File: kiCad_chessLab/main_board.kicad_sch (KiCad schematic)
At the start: 3 parts, among them IC1 ESP32-C6-WROOM-1-N8, J1 TYPE-C-31-M-12

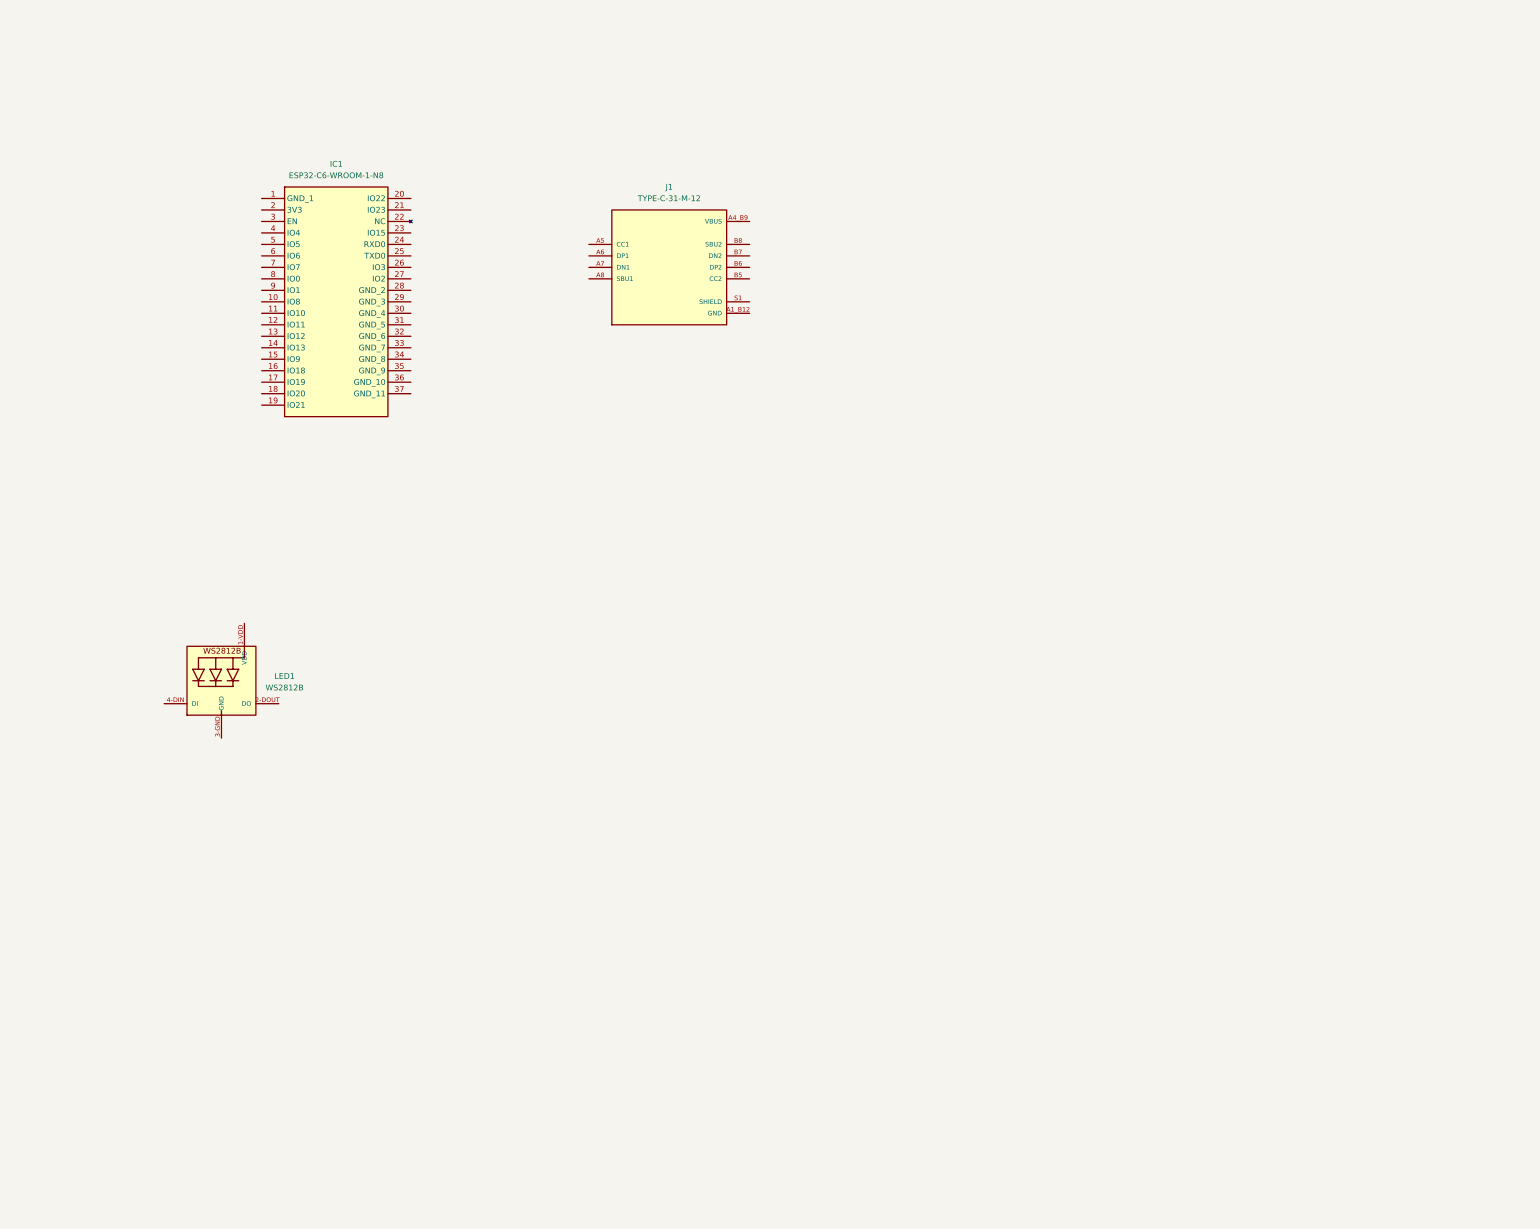
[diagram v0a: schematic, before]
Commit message: Creation des Cellules et Fonctions de Multiplexage
Organisation du projet KiCad en SousPages

Creation des Fonctions Cell: Gestion individuelle de une case

Row: Multiplexage de 8 cell

Main Board:
Liaisons avec ESP32C6
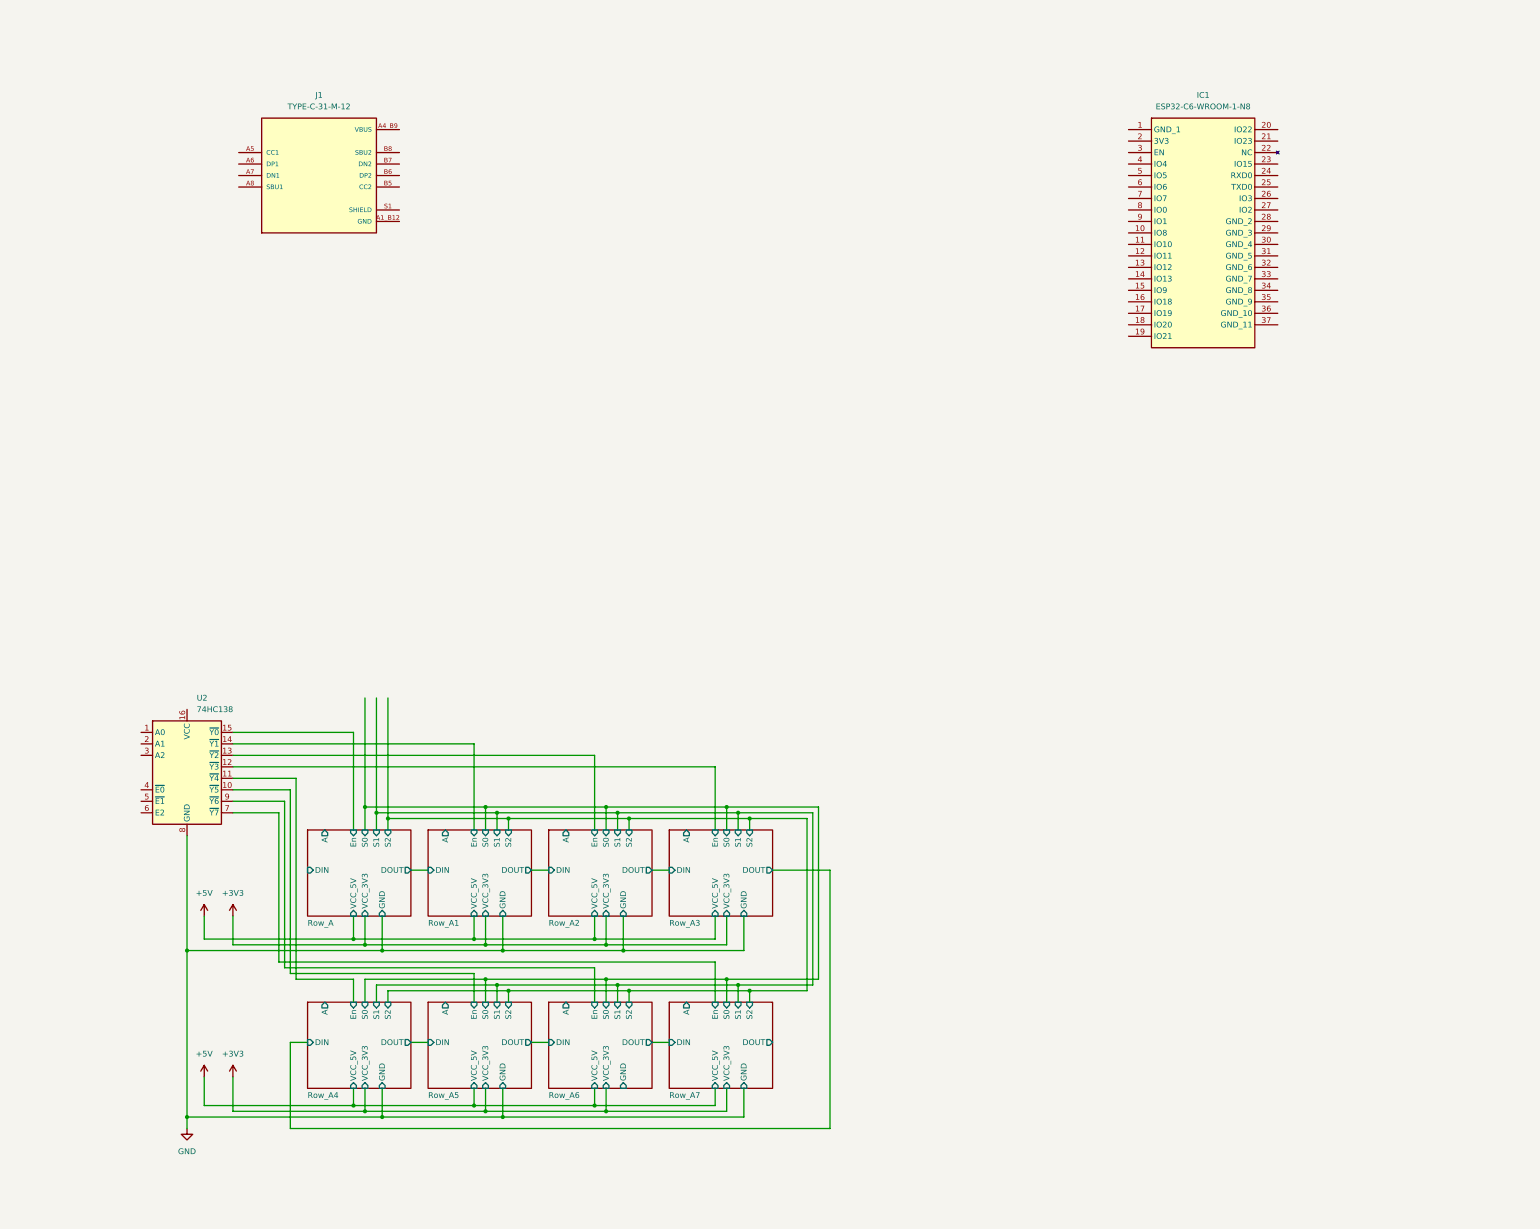
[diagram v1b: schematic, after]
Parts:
- removed LED1: WS2812B, symbol chessLab-symbols:WS2812B
- added U2: 74HC138, Package_SO:SOIC-16_3.9x9.9mm_P1.27mm, symbol 74xx:74HC138
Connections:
- net GND: now also U2.8 (GND)
- new net Row_A/En: U2.15 (~{Y0})
- new net Row_A1/En: U2.14 (~{Y1})
- new net Row_A2/En: U2.13 (~{Y2})
- new net Row_A3/En: U2.12 (~{Y3})
- new net Row_A4/En: U2.11 (~{Y4})
- new net Row_A5/En: U2.10 (~{Y5})
- new net Row_A6/En: U2.9 (~{Y6})
- new net Row_A7/En: U2.7 (~{Y7})
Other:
- added sheet Row_A (row.kicad_sch)
- added sheet Row_A1 (row.kicad_sch)
- added sheet Row_A2 (row.kicad_sch)
- added sheet Row_A3 (row.kicad_sch)
- added sheet Row_A4 (row.kicad_sch)
- added sheet Row_A5 (row.kicad_sch)
- added sheet Row_A6 (row.kicad_sch)
- added sheet Row_A7 (row.kicad_sch)
- moved on the sheet: IC1, J1

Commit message: KiCad Bug Fix
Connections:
- net +3V3: now also U2.16 (VCC)
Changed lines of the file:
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@@
+	(wire
+		(pts
+			(xy 53.34 163.83) (xy 53.34 170.18)
+		)
+		(stroke
+			(width 0)
+			(type default)
+		)
+	)
 	(wire
 		(pts
@@
 		)
 	)
+	(symbol
+		(lib_id "power:+3V3")
+		(at 53.34 163.83 0)
+		(unit 1)
+		(exclude_from_sim no)
+		(in_bom yes)
+		(on_board yes)
+		(dnp no)
+		(fields_autoplaced yes)
+		(property "Reference" "#PWR06"
+			(at 53.34 167.64 0)
+			(effects
+				(font
+					(size 1.27 1.27)
+				)
+				(hide yes)
+			)
+		)
+		(property "Value" "+3V3"
+			(at 53.34 158.75 0)
+			(effects
+				(font
+					(size 1.27 1.27)
+				)
+			)
+		)
+		(property "Footprint" ""
+			(at 53.34 163.83 0)
+			(effects
+				(font
+					(size 1.27 1.27)
+				)
+				(hide yes)
+			)
+		)
+		(property "Datasheet" ""
+			(at 53.34 163.83 0)
+			(effects
+				(font
+					(size 1.27 1.27)
+				)
+				(hide yes)
+			)
+		)
+		(property "Description" "Power symbol creates a global label with name \"+3V3\""
+			(at 53.34 163.83 0)
+			(effects
+				(font
+					(size 1.27 1.27)
+				)
+				(hide yes)
+			)
+		)
+		(pin "1"
+		)
+		(instances
+			(project "kiCad_chessLab"
+				(path "/767acb05-88fd-4294-8dd3-73f8ac75b0d1/879e1270-2f10-48e2-adb9-8c8e9c331030"
+					(reference "#PWR06")
+					(unit 1)
+				)
+			)
+		)
+	)

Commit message: Main Board update
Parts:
- added BOOT, RST: B3U-1000P, B3U-1000P, symbol chessLab-symbols:B3U-1000P
- added C66: 100nF, Capacitor_SMD:C_0603_1608Metric_Pad1.08x0.95mm_HandSolder, symbol Device:C
- added C67: 100uF, Capacitor_SMD:C_0603_1608Metric_Pad1.08x0.95mm_HandSolder, symbol Device:C
- added C68: 10uF, Capacitor_SMD:C_0603_1608Metric_Pad1.08x0.95mm_HandSolder, symbol Device:C
- added J2: PWR, CONN4_1048_KEY, symbol chessLab-symbols:1048
- added J3: DATA, CONN4_1048_KEY, symbol chessLab-symbols:1048
- added R1: 33, Resistor_SMD:R_0603_1608Metric_Pad0.98x0.95mm_HandSolder, symbol Device:R
- added R11, R8: 100k, Resistor_SMD:R_0603_1608Metric_Pad0.98x0.95mm_HandSolder, symbol Device:R
- added R115, R116: 5.1k, Resistor_SMD:R_0603_1608Metric_Pad0.98x0.95mm_HandSolder, symbol Device:R
- added R2, R4, R6: 10k, Resistor_SMD:R_0603_1608Metric_Pad0.98x0.95mm_HandSolder, symbol Device:R
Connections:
- net +3V3: now also IC1.2 (3V3), U2.6 (E2), C66.2, C67.2, C68.2, J2.3, R2.2, R4.2
- net +5V: now also J2.2
- net GND: now also IC1.1 (GND_1), IC1.28 (GND_2), IC1.29 (GND_3), IC1.30 (GND_4), IC1.31 (GND_5), IC1.32 (GND_6), IC1.33 (GND_7), IC1.34 (GND_8), IC1.35 (GND_9), IC1.36 (GND_10), IC1.37 (GND_11), J1.S1 (SHIELD), J1.S2 (SHIELD), J1.S3 (SHIELD), J1.S4 (SHIELD), U2.4 (~{E0}), U2.5 (~{E1}), BOOT.2 (A), C66.1, C67.1, C68.1, J2.4, J3.4, R11.1, R115.2, R116.1, R6.2, RST.2 (A)
- net Row_A/DIN: now also R1.2
- net VBUS: now also J2.1
- net A0: now reaches U2.1 (A0)
- net A0: now also IC1.26 (IO3)
- net A1: now reaches U2.2 (A1)
- net A1: now also IC1.21 (IO23), IC1.25 (TXD0)
- net A2: now reaches U2.3 (A2)
- net A2: now also IC1.24 (RXD0)
- net at J1.A5 (CC1): now also R116.2
- net GPIO13: now reaches J1.A6 (DP1)
- net GPIO13: now also IC1.14 (IO13), J1.B6 (DP2)
- net GPIO12: now reaches J1.A7 (DN1)
- net GPIO12: now also IC1.13 (IO12), J1.B7 (DN2)
- net at J1.B5 (CC2): now also R115.1
- net at IC1.15 (IO9): now also BOOT.1 (K), R4.1
- net A_OUT: now reaches IC1.16 (IO18)
- net DIN: now reaches IC1.17 (IO19)
- net DIN: now also R1.1
- net at IC1.18 (IO20): now also R11.2, R8.1
- net BTN_PWR: now reaches IC1.19 (IO21)
- net BTN_PWR: now also J3.2, R6.1
- net PWR_HOLD: now reaches IC1.20 (IO22)
- net PWR_HOLD: now also J3.1
- net S2: now reaches IC1.27 (IO2)
- net at IC1.3 (EN): now also R2.1, RST.1 (K)
- net S0: now reaches IC1.8 (IO0)
- net S1: now reaches IC1.9 (IO1)
- new net VBAT: J3.3, R8.2
- no-connect marks 0 -> 9
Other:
- sheet Row_A1 renamed Row_B
- sheet Row_A2 renamed Row_C
- sheet Row_A3 renamed Row_D
- sheet Row_A4 renamed Row_E
- sheet Row_A5 renamed Row_F
- sheet Row_A6 renamed Row_G
- sheet Row_A7 renamed Row_H
- note added: "CONNECTEUR USB-C"
- note added: "GESTION DES ROW"
- moved on the sheet: IC1, J1, U2

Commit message: Complete Schematics
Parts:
- added TP11: GND, TestPoint:TestPoint_Plated_Hole_D2.0mm, symbol Connector:TestPoint
- added TP12: SW_RST, TestPoint:TestPoint_Plated_Hole_D2.0mm, symbol Connector:TestPoint
- SW2: renamed from RST; value B3U-1000P -> RST
- SW3: renamed from BOOT; value B3U-1000P -> BOOT
- renumbered C68 to C10, C66 to C8, C67 to C9, IC1 to IC4, J1 to J4, J3 to J5, J2 to J6, R116 to R10, R1 to R11, R115 to R12, R2 to R13, R4 to R14, R6 to R15, R8 to R16, R11 to R17, U2 to U3
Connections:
- net GND: now also TP11.1
- net at IC4.3 (EN), R13.1, SW2.1 (K): now also TP12.1
- no-connect marks 9 -> 11
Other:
- note added: "CONNECTORS"
- note added: "ESP32C6"
- moved on the sheet: C10, C8, C9, IC4, J4, J5, J6, R10, R11, R12, R13, R14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

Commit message: PCB SetUp
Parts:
- J4: footprint TYPE-C-31-M-12:HRO_TYPE-C-31-M-12 -> chessLab-footprints:HRO_TYPE-C-31-M-12
- J5, J6: footprint CONN4_1048_KEY -> Connector_JST:JST_XH_B4B-XH-A_1x04_P2.50mm_Vertical
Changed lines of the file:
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@@
 			)
 		)
-		(property "Footprint" "CONN4_1048_KEY"
+		(property "Footprint" "Connector_JST:JST_XH_B4B-XH-A_1x04_P2.50mm_Vertical"
 			(at 48.26 147.32 0)
 			(effects
@@
 			)
 		)
-		(property "Footprint" "CONN4_1048_KEY"
+		(property "Footprint" "Connector_JST:JST_XH_B4B-XH-A_1x04_P2.50mm_Vertical"
 			(at 48.26 172.72 0)
 			(effects
@@
 			)
 		)
-		(property "Footprint" "TYPE-C-31-M-12:HRO_TYPE-C-31-M-12"
+		(property "Footprint" "chessLab-footprints:HRO_TYPE-C-31-M-12"
 			(at 118.11 171.45 0)
 			(effects

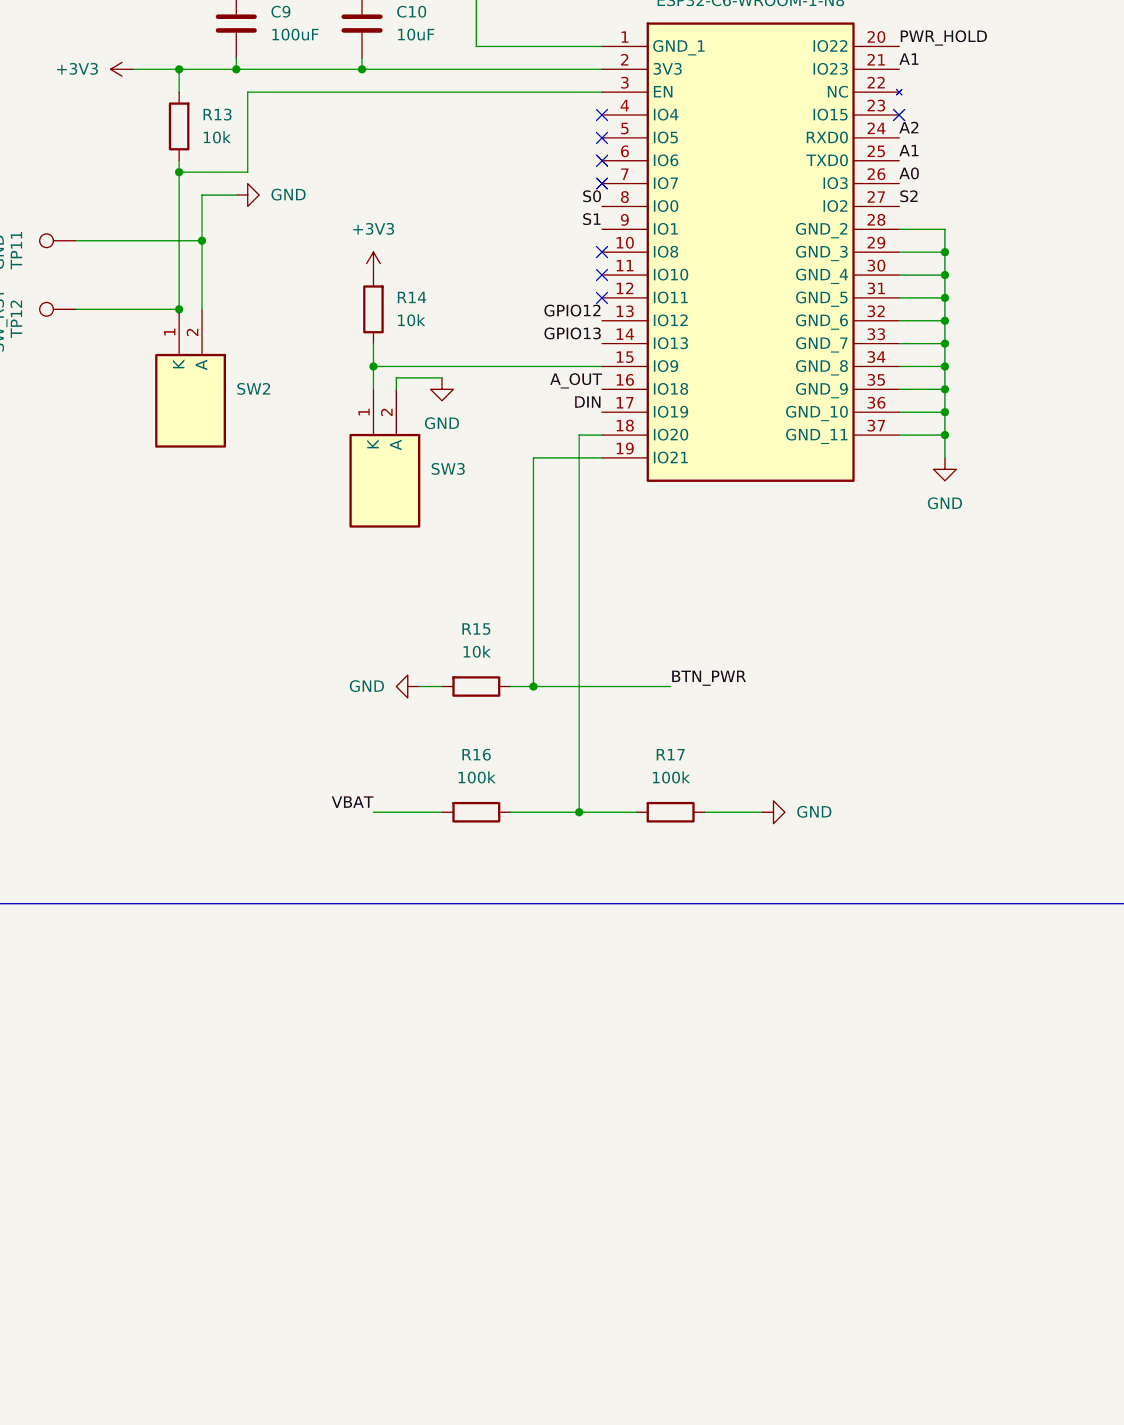
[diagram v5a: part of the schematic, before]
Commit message: Hall effect Replaced and 3d files uploaded
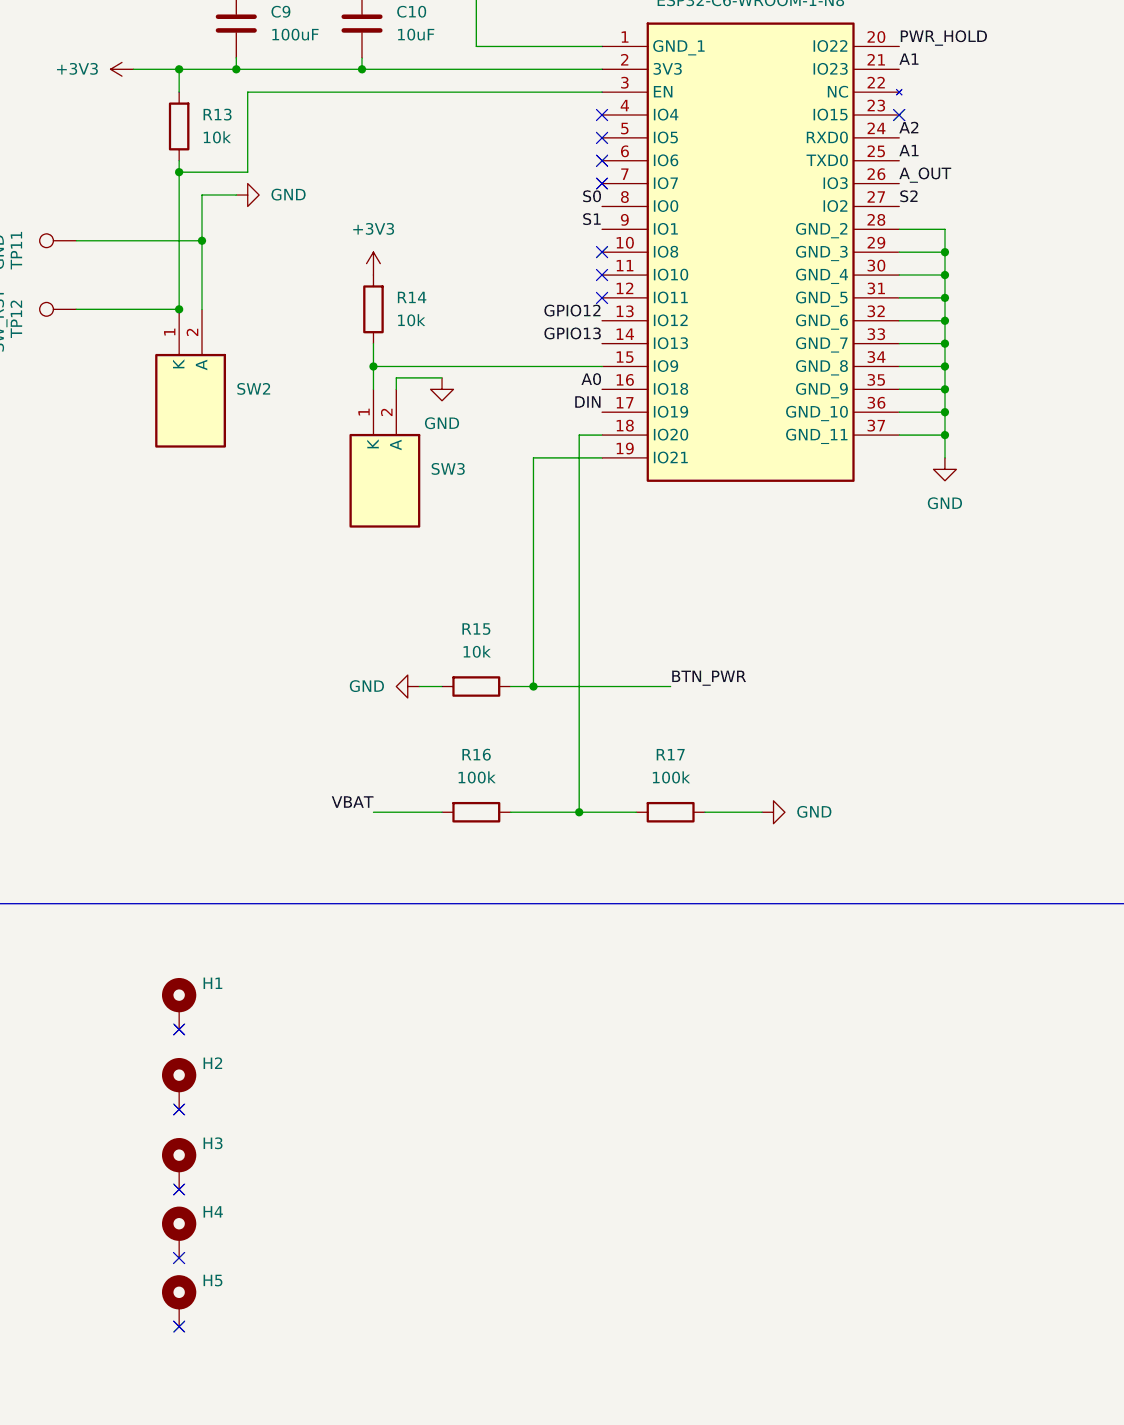
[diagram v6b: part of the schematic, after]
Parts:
- added H1, H2, H3, H4, H5: MountingHole_Pad, MountingHole:MountingHole_2.2mm_M2_DIN965_Pad, symbol Mechanical:MountingHole_Pad
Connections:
- net A0: now also IC4.16 (IO18); no longer IC4.26 (IO3)
- net A_OUT: now also IC4.26 (IO3); no longer IC4.16 (IO18)
- no-connect marks 11 -> 16

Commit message: aa
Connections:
- net GPIO12 renamed DN
- net GPIO13 renamed DP
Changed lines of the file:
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@@
 		)
 	)
-	(label "GPIO12"
+	(label "DN"
 		(at 275.59 72.39 180)
 		(effects
@@
 		)
 	)
-	(label "GPIO12"
+	(label "DN"
 		(at 135.89 168.91 0)
 		(effects
@@
 		)
 	)
-	(label "GPIO12"
+	(label "DN"
 		(at 100.33 171.45 180)
 		(effects
@@
 		)
 	)
-	(label "GPIO13"
+	(label "DP"
 		(at 100.33 168.91 180)
 		(effects
@@
 		)
 	)
-	(label "GPIO13"
+	(label "DP"
 		(at 275.59 74.93 180)
 		(effects
@@
 		)
 	)
-	(label "GPIO13"
+	(label "DP"
 		(at 135.89 171.45 0)
 		(effects
